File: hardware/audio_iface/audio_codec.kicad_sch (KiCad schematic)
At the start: 1 part, among them U301 SGTL5000XNAA3

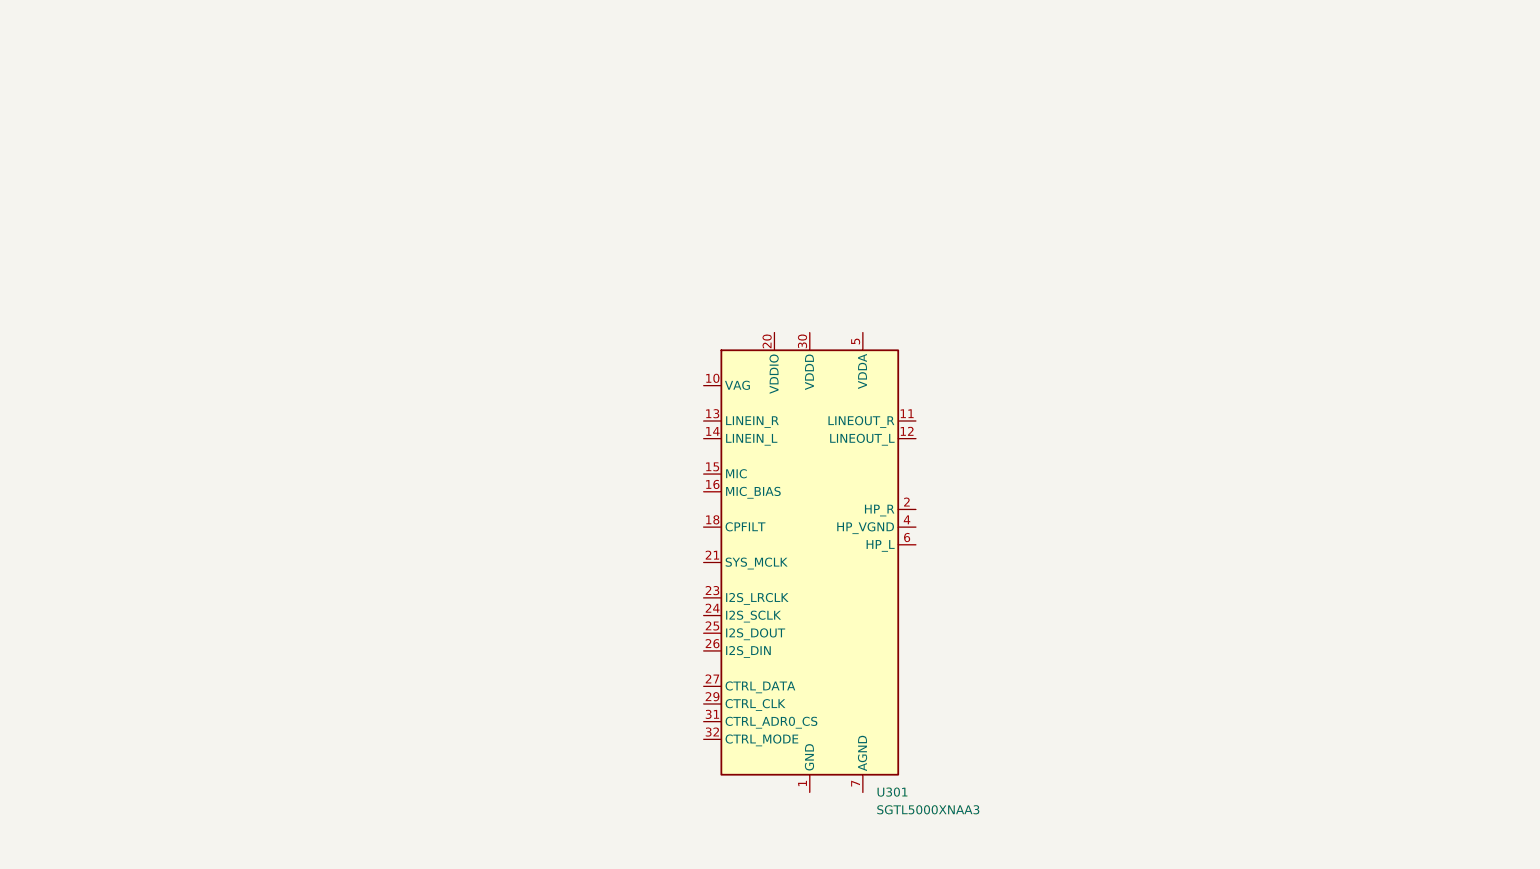
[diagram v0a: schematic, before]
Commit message: added some connections
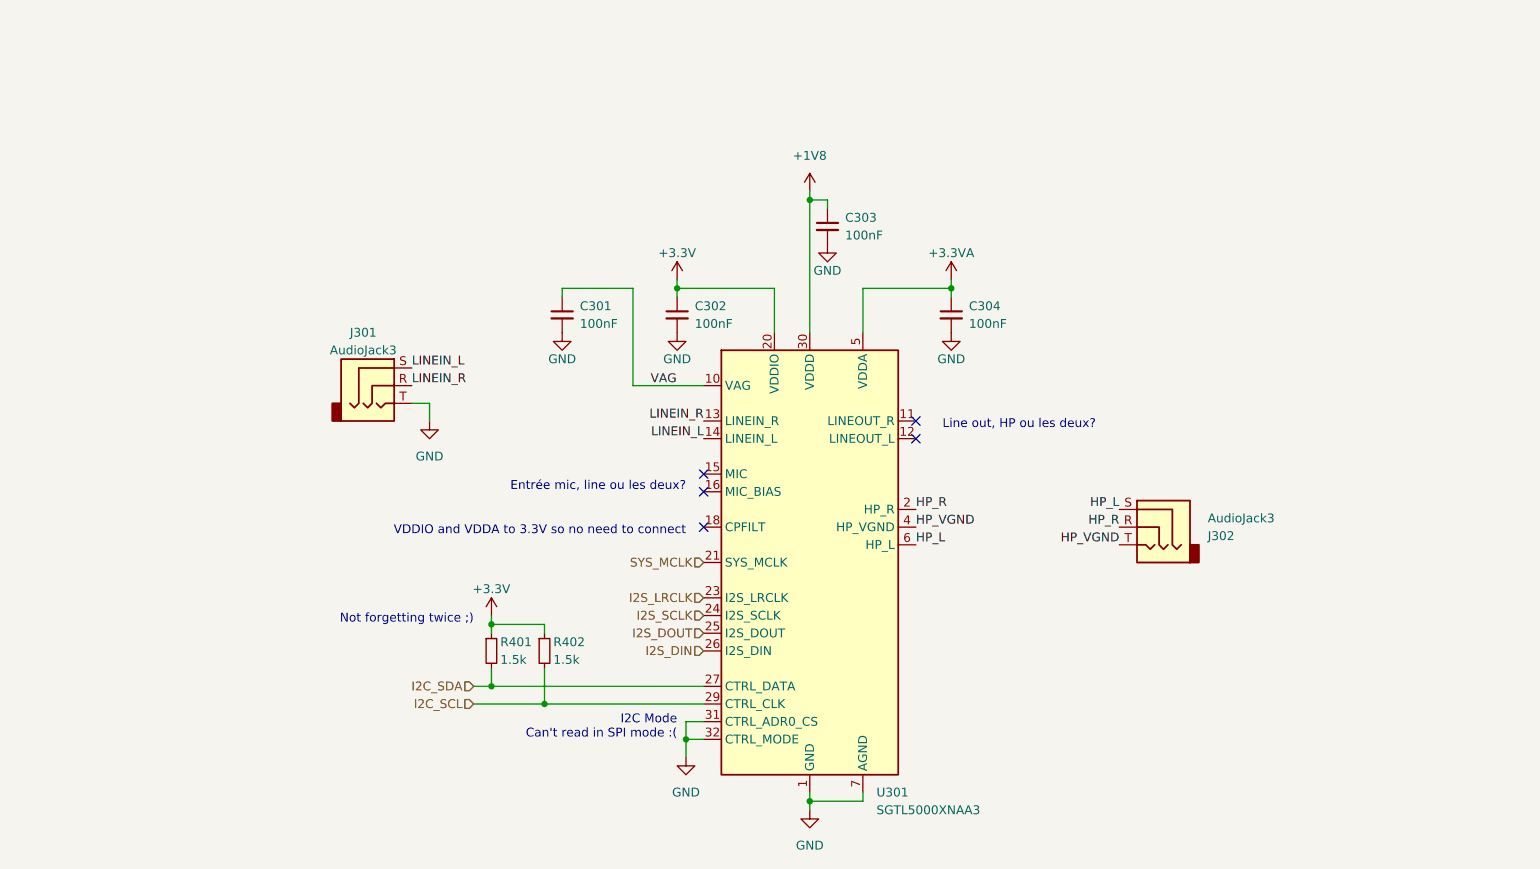
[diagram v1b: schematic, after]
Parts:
- added C301, C302, C303, C304: 100nF, Capacitor_SMD:C_0402_1005Metric, symbol Device:C_Small
- added J301, J302: AudioJack3, symbol Connector_Audio:AudioJack3
- added R401, R402: 1.5k, Resistor_SMD:R_0402_1005Metric, symbol Device:R_Small
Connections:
- net GND: now reaches U301.1 (GND), U301.3 (GND), U301.33 (GND)
- net GND: now also U301.31 (CTRL_ADR0_CS), U301.32 (CTRL_MODE), U301.7 (AGND), C301.2, C302.2, C303.2, C304.2, J301.T
- net VAG: now reaches U301.10 (VAG)
- net VAG: now also C301.1
- net LINEIN_R: now reaches U301.13 (LINEIN_R)
- net LINEIN_R: now also J301.R
- net LINEIN_L: now reaches U301.14 (LINEIN_L)
- net LINEIN_L: now also J301.S
- net HP_R: now reaches U301.2 (HP_R)
- net HP_R: now also J302.R
- net +3V3: now reaches U301.20 (VDDIO)
- net +3V3: now also C302.1, R401.1, R402.1
- net SYS_MCLK: now reaches U301.21 (SYS_MCLK)
- net I2S_LRCLK: now reaches U301.23 (I2S_LRCLK)
- net I2S_SCLK: now reaches U301.24 (I2S_SCLK)
- net I2S_DOUT: now reaches U301.25 (I2S_DOUT)
- net I2S_DIN: now reaches U301.26 (I2S_DIN)
- net I2C_SDA: now reaches U301.27 (CTRL_DATA)
- net I2C_SDA: now also R401.2
- net I2C_SCL: now reaches U301.29 (CTRL_CLK)
- net I2C_SCL: now also R402.2
- net +1V8: now reaches U301.30 (VDDD)
- net +1V8: now also C303.1
- net HP_VGND: now reaches U301.4 (HP_VGND)
- net HP_VGND: now also J302.T
- net +3.3VA: now reaches U301.5 (VDDA)
- net +3.3VA: now also C304.1
- net HP_L: now reaches U301.6 (HP_L)
- net HP_L: now also J302.S
- no-connect marks 0 -> 5
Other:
- note added: "Entrée mic, line ou les deux?"
- note added: "I2C Mode Can't read in SPI mode :("
- note added: "Line out, HP ou les deux?"
- note added: "Not forgetting twice ;)"
- note added: "VDDIO and VDDA to 3.3V so no need to connect"

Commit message: Added LEDs
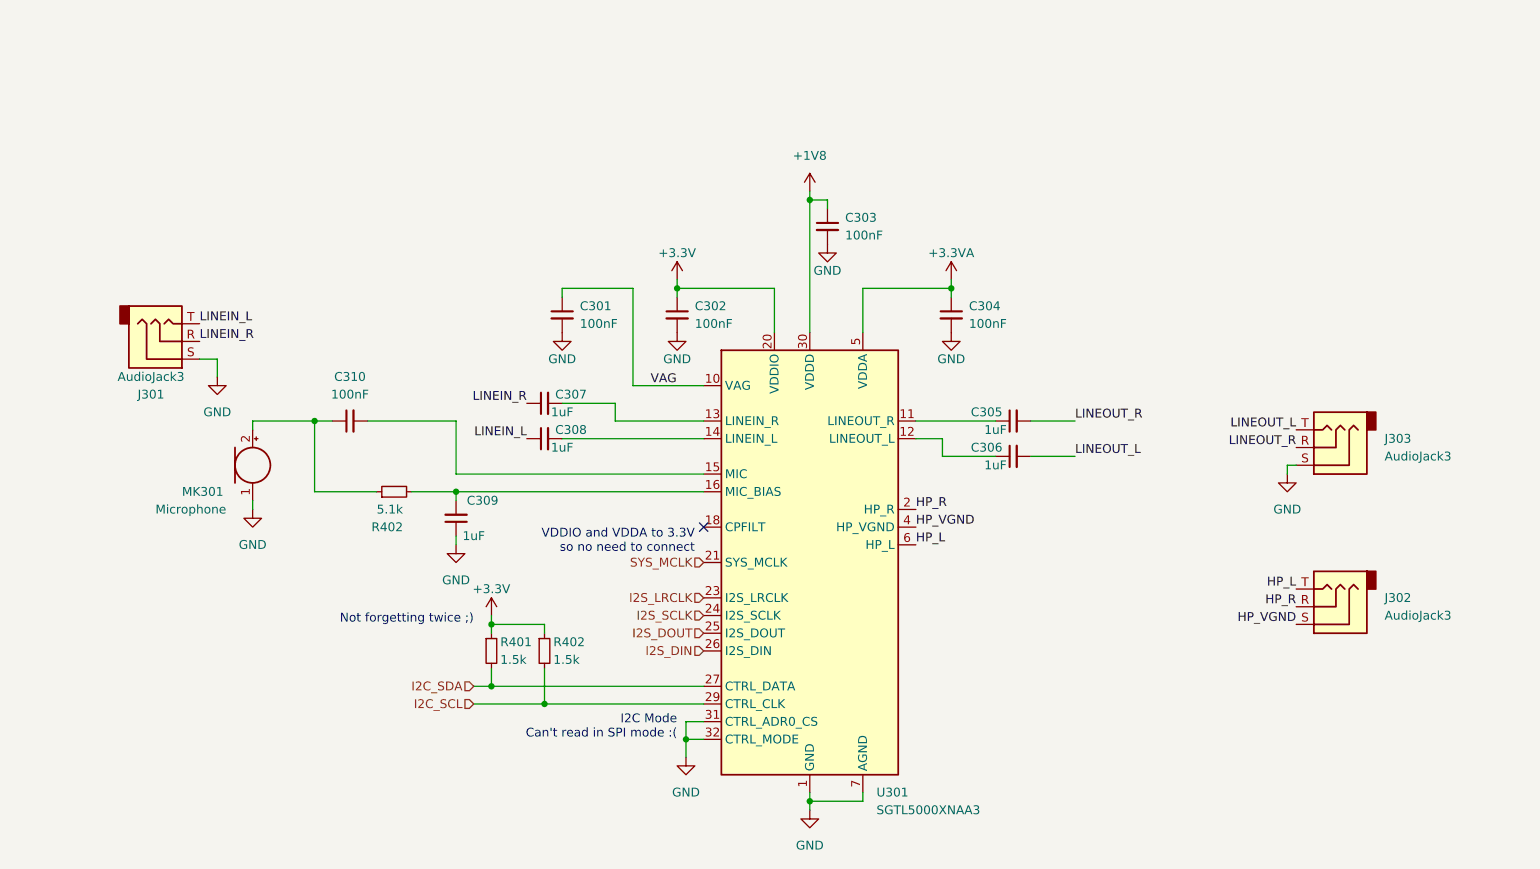
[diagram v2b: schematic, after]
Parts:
- added C305, C306, C307, C308, C309: 1uF, Capacitor_SMD:C_0603_1608Metric, symbol Device:C_Small
- added C310: 100nF, Capacitor_SMD:C_0402_1005Metric, symbol Device:C_Small
- added J303: AudioJack3, symbol Connector_Audio:AudioJack3
- added MK301: Microphone, symbol Device:Microphone
- added R402: 5.1k, Resistor_SMD:R_0402_1005Metric, symbol Device:R_Small
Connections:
- net GND: now also J301.S, C309.1, J303.S, MK301.1 (-); no longer J301.T
- net HP_L: now also J302.T; no longer J302.S
- net HP_VGND: now also J302.S; no longer J302.T
- net LINEIN_L: now also J301.T, C308.1; no longer J301.S, U301.14 (LINEIN_L)
- net LINEIN_R: now also C307.1; no longer U301.13 (LINEIN_R)
- net at U301.11 (LINEOUT_R): now also C305.1
- net at U301.12 (LINEOUT_L): now also C306.1
- net at U301.15 (MIC): now also C310.2
- net at U301.16 (MIC_BIAS): now also C309.2, R402.2
- new net: C310.1, MK301.2 (+), R402.1
- new net: C308.2, U301.14 (LINEIN_L)
- new net: C307.2, U301.13 (LINEIN_R)
- new net LINEOUT_L: C306.2, J303.T
- new net LINEOUT_R: C305.2, J303.R
- no-connect marks 5 -> 1
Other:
- note removed: "Entrée mic, line ou les deux?"
- note removed: "Line out, HP ou les deux?"
- moved on the sheet: J301, J302

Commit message: schematic v1 done
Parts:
- removed J301, J302, J303: AudioJack3, symbol Connector_Audio:AudioJack3
- added J301, J302, J303: AudioJack4, Connector_Audio:Jack_3.5mm_PJ320D_Horizontal, symbol Connector_Audio:AudioJack4
- added TP301, TP302, TP303, TP304, TP305: TestPoint, Connector_Pin:Pin_D1.1mm_L8.5mm_W2.5mm_FlatFork, symbol Connector:TestPoint
- MK301: footprint (none) -> WITNS:Electret_ABM-713-RC; Farnell (none) -> 2066499
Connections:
- net GND: now also J301.S, J303.S
- net HP_L: now also J302.T
- net HP_R: now also J302.R1
- net HP_VGND: now also J302.S
- net LINEIN_L: now also C307.2, U301.14 (LINEIN_L), TP303.1; no longer C308.1
- net LINEIN_R: now also C308.2, U301.13 (LINEIN_R), TP302.1; no longer C307.1
- net LINEOUT_L: now also C305.1, U301.12 (LINEOUT_L), TP305.1; no longer C306.2
- net LINEOUT_R: now also C306.1, U301.11 (LINEOUT_R), TP304.1; no longer C305.2
- net at C310.2, U301.15 (MIC): now also TP301.1
- new net: C308.1, J301.R1
- new net: C307.1, J301.T
- new net: C306.2, J303.R1
- new net: C305.2, J303.T
- no-connect marks 1 -> 4
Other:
- moved on the sheet: C305, C306, C307, C308

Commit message: routing v1
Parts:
- added TP306: R, Connector_Pin:Pin_D1.1mm_L8.5mm_W2.5mm_FlatFork, symbol Connector:TestPoint
- added TP307: HP GND, Connector_Pin:Pin_D1.1mm_L8.5mm_W2.5mm_FlatFork, symbol Connector:TestPoint
- added TP308: L, Connector_Pin:Pin_D1.1mm_L8.5mm_W2.5mm_FlatFork, symbol Connector:TestPoint
- J301: value AudioJack4 -> LINEIN
- J302: value AudioJack4 -> HP
- J303: value AudioJack4 -> LINEOUT
- TP301: value TestPoint -> MIC
- TP302, TP304: value TestPoint -> R
- TP303, TP305: value TestPoint -> L
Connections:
- net HP_L: now also TP308.1
- net HP_R: now also TP306.1
- net HP_VGND: now also TP307.1
- net MIC: now reaches C310.2, TP301.1, U301.15 (MIC)
- net MIC_BIAS: now reaches C309.2, R402.2, U301.16 (MIC_BIAS)
- net +3V3 renamed +3.3V

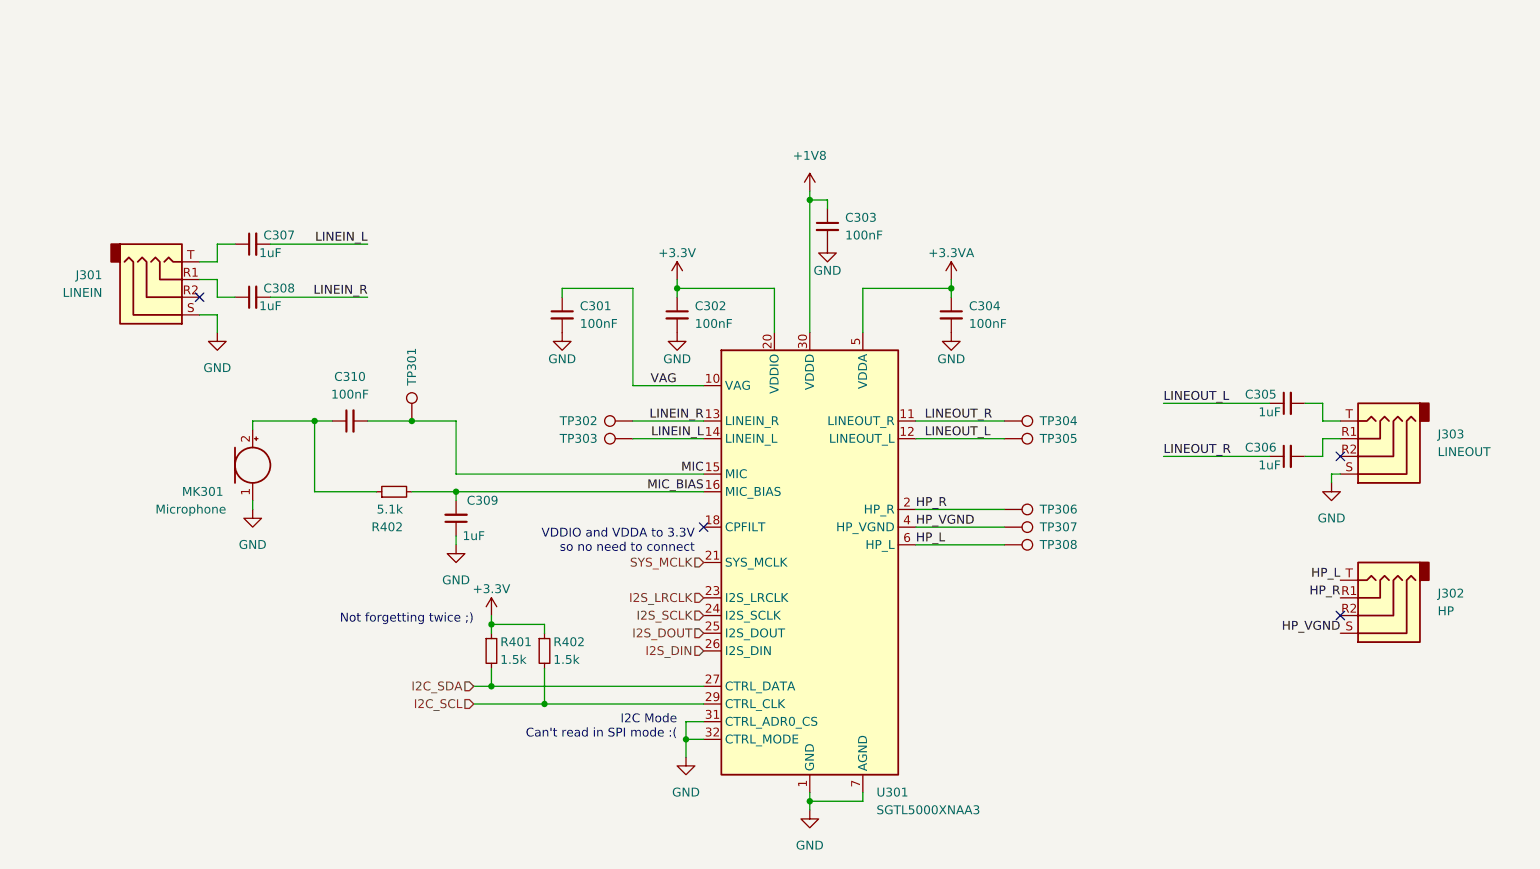
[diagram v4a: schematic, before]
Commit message: add logo
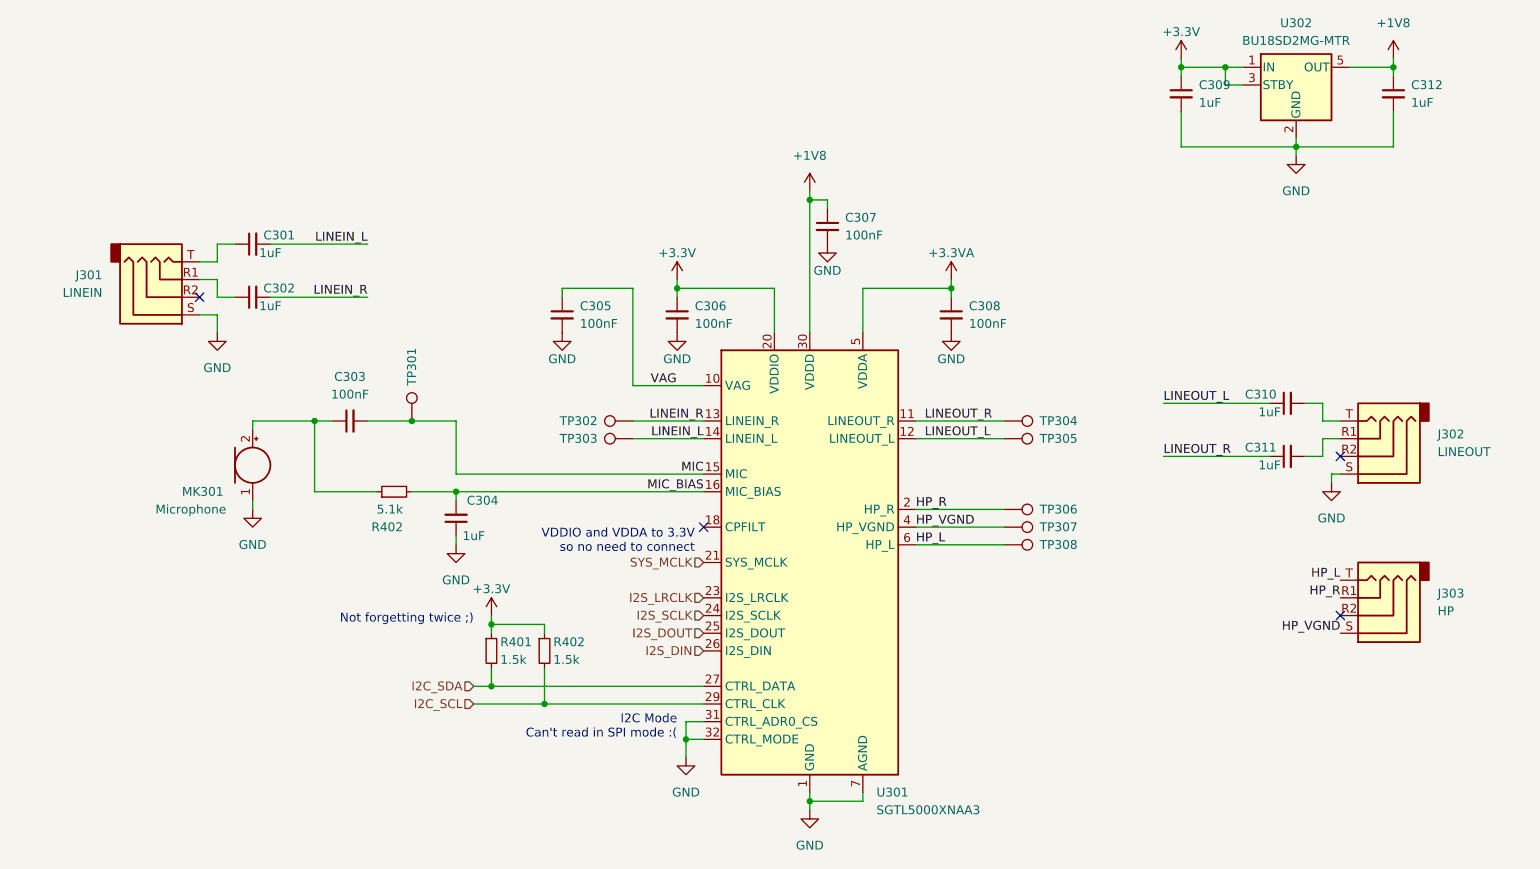
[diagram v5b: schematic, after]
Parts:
- added C309, C312: 1uF, Capacitor_SMD:C_0603_1608Metric, symbol Device:C_Small
- added U302: BU18SD2MG-MTR, Package_TO_SOT_SMD:SOT-23-5, symbol WITNS_ROHM:BU18SD2MG-MTR
- C301: renamed from C307; LCSC Part (none) -> C15849
- C302: renamed from C308; LCSC Part (none) -> C15849
- C303: renamed from C310; LCSC Part (none) -> C1525
- C304: renamed from C309; LCSC Part (none) -> C15849
- C305: renamed from C301; LCSC Part (none) -> C1525
- C306: renamed from C302; LCSC Part (none) -> C1525
- C307: renamed from C303; LCSC Part (none) -> C1525
- C308: renamed from C304; LCSC Part (none) -> C1525
- C310: renamed from C305; LCSC Part (none) -> C15849
- C311: renamed from C306; LCSC Part (none) -> C15849
- R402: LCSC Part (none) -> C2906948
- renumbered J303 to J302, J302 to J303
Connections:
- net +1V8: now also C312.1, U302.5 (OUT)
- net +3.3V: now also C309.1, U302.1 (IN), U302.3 (STBY)
- net GND: now also C309.2, C312.2, U302.2 (GND)
